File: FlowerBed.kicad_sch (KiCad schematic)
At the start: 28 parts, among them J1 Conn_01x02, J2 AudioJack3_SwitchTR, J3 AudioJack3_SwitchTR, J4 Conn_01x07, J5 Conn_01x16, J6 Conn_01x02, SW0 SW_SPST, SW1 SW_SPST, SW2 SW_SPST, SW3 SW_SPST, SW4 SW_SPST, SW5 SW_SPST, SW6 SW_SPST, SW7 SW_SPST, U1 PAM8302AASCR

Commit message: Legacy active sum
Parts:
- removed R1, R2: 1k, Resistor_SMD:R_01005_0402Metric, symbol Device:R_US
- added C5, C6, C7: 1uF, symbol Device:C
- added C8: 100n, symbol Device:C
- added J7: USB_C_Receptacle_PowerOnly_6P, symbol Connector:USB_C_Receptacle_PowerOnly_6P
- added R10, R7, R8, R9: 20k, Resistor_SMD:R_01005_0402Metric, symbol Device:R_US
- added R12: 1Meg, Resistor_SMD:R_01005_0402Metric, symbol Device:R_US
- added R13: 50, Resistor_SMD:R_01005_0402Metric, symbol Device:R_US
- added R14: 10k, Resistor_SMD:R_01005_0402Metric, symbol Device:R_US
- added R4: 150, symbol Device:R_US
- added R5, R6: 5.1k, symbol Device:R_US
- added U2: TPS2115ADRBR, Package_TO_SOT_SMD:SOT-583-8, symbol Flowerbed:TPS2115ADRBR
- added U4: TLV271CDBVR, Package_TO_SOT_SMD:SOT-353_SC-70-5, symbol Amplifier_Operational:TLV172IDCK
- A1, J1, J2, J3, J4, J5, J6, POT0, POT1, POT2, POT3, SW0, SW1, SW2, SW3, SW4, SW5, SW6, SW7: now fitted
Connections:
- net 3V3_A: now also C6.1, R9.2, U2.2 (D0), U2.8 (IN1), U4.5 (V+)
- net GND: now also C5.2, C6.2, C7.2, J7.A12 (GND), J7.B12 (GND), J7.S1 (SHIELD), R10.1, R12.1, R4.2, R5.1, R6.1, U2.3 (D1), U2.5 (GND), U4.2 (V-)
- net LINEOUT_MONO: now also R13.1
- net Vin: now also C7.1, J7.A9 (VBUS), J7.B9 (VBUS), U2.7 (OUT)
- net at J2.RN: now also R8.2
- net at J2.TN: now also R7.2
- new net: C8.2, R13.2
- new net: R4.1, U2.4 (ILIM)
- new net: R14.2, R7.1, R8.1, U4.1 (+)
- new net: C8.1, R12.2, U4.3 (-), U4.4
- new net: J7.A5 (CC1), R5.2
- new net: J7.B5 (CC2), R6.2
- new net 1v65: R10.2, R14.1, R9.1
- new net IN_5V: C5.1, U2.6 (IN2)
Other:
- note added: "5V USB-C Input & Power Mux"
- note added: "Audio I/O & Mono Summing Amp"
- note added: "Class-D Amp"
- note added: "Daisy Breakouts"
- note added: "GPIO"
- moved on the sheet: C1, C2, C3, R3, U1, VR1

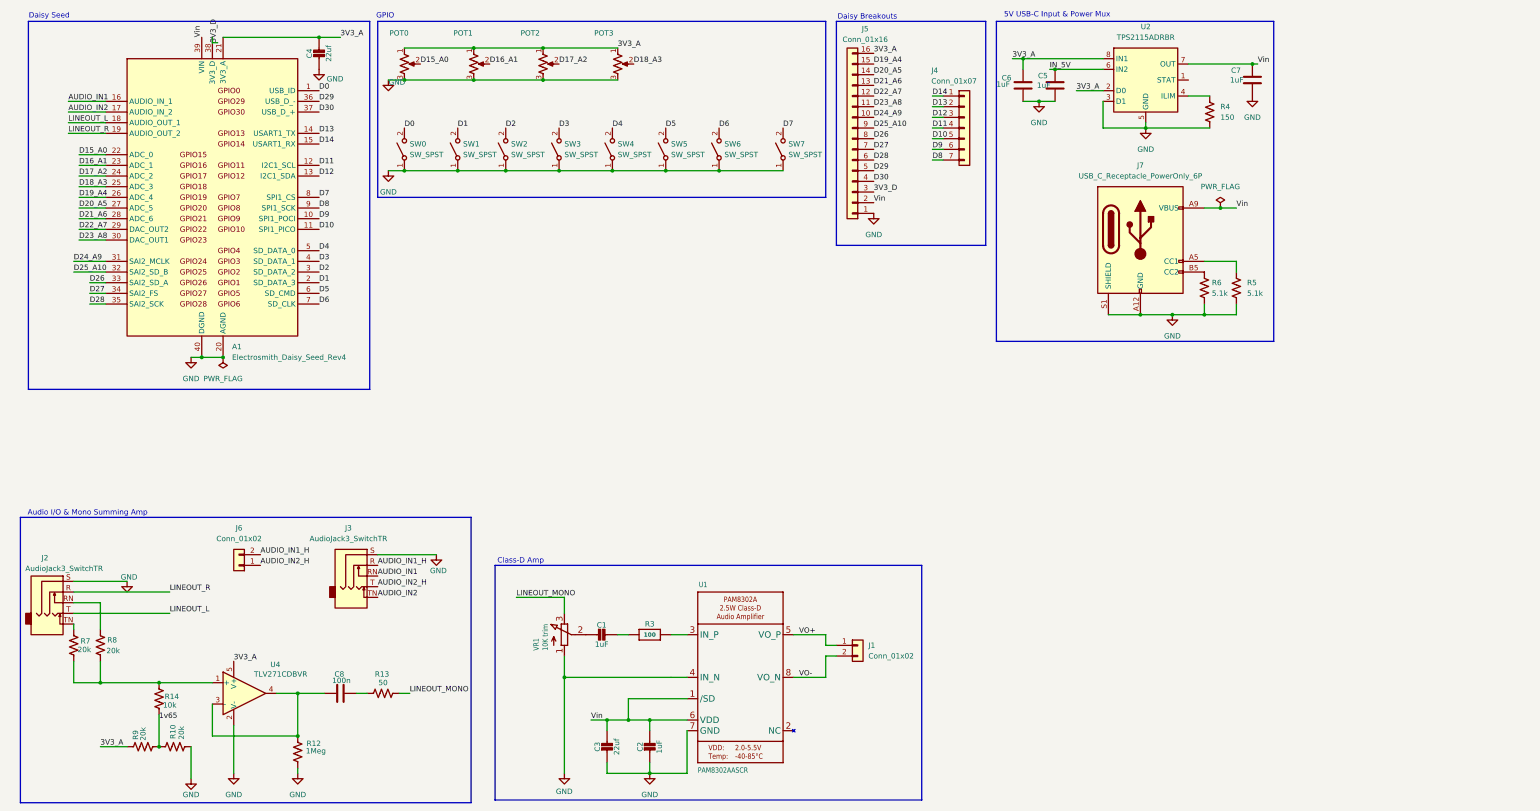
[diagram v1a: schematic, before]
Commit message: Make sum passive, add manuals
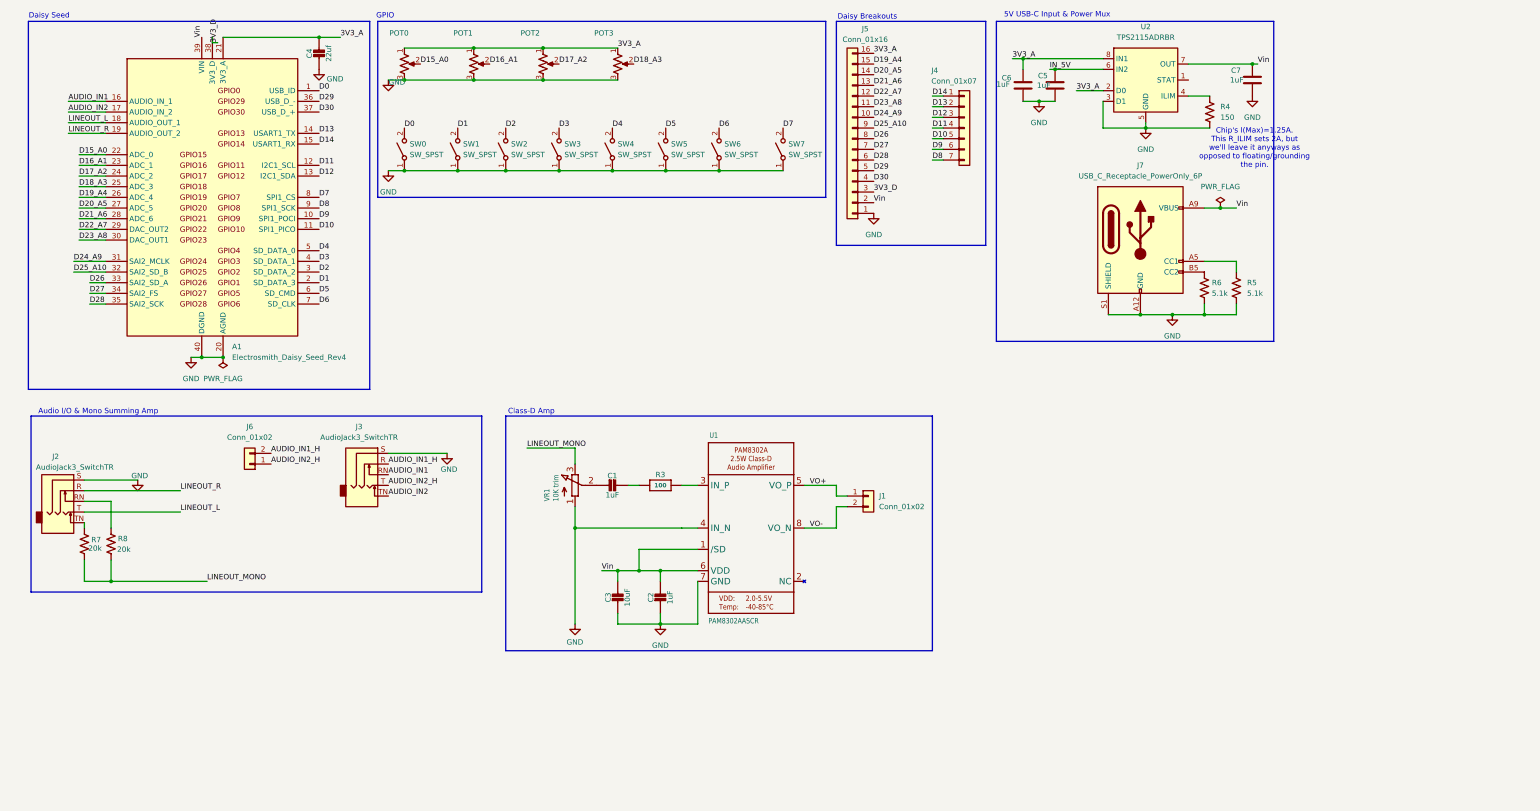
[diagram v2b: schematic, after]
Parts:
- removed C8: 100n, symbol Device:C
- removed R10, R9: 20k, Resistor_SMD:R_01005_0402Metric, symbol Device:R_US
- removed R12: 1Meg, Resistor_SMD:R_01005_0402Metric, symbol Device:R_US
- removed R13: 50, Resistor_SMD:R_01005_0402Metric, symbol Device:R_US
- removed R14: 10k, Resistor_SMD:R_01005_0402Metric, symbol Device:R_US
- removed U4: TLV271CDBVR, Package_TO_SOT_SMD:SOT-353_SC-70-5, symbol Amplifier_Operational:TLV172IDCK
- C3: value 22uf -> 10uF
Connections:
- net LINEOUT_MONO: now also R7.1, R8.1
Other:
- note added: "Chip's I(Max)=1.25A. This R_ILIM sets 2A, but we'll leave it anyways as opposed to floating/grounding the pin."
- moved on the sheet: C1, C2, C3, J1, J2, J3, J6, R3, R7, R8, U1, VR1

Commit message: Update footprints for ICs
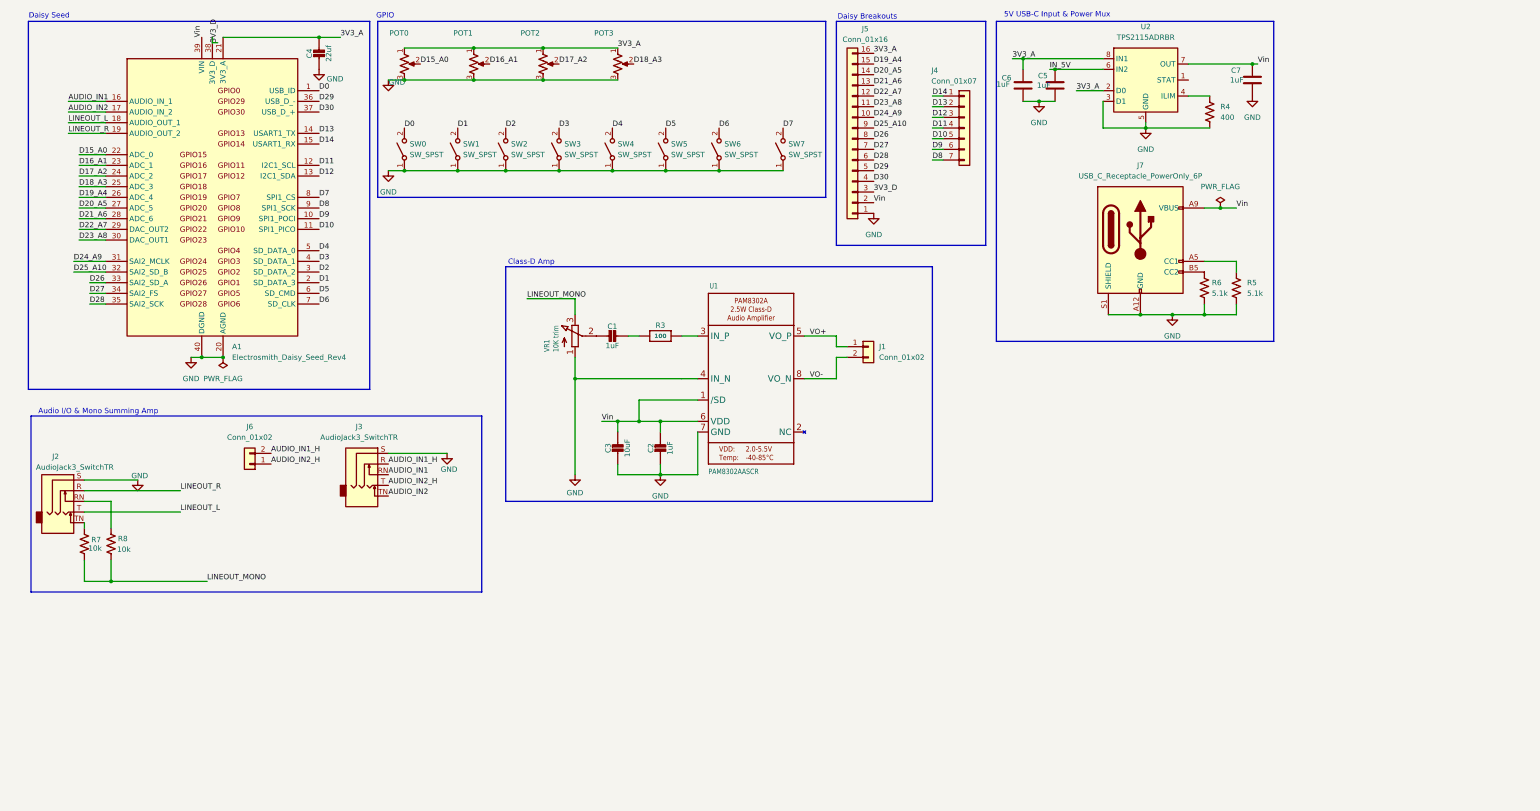
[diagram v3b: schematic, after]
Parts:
- J7: footprint (none) -> Flowerbed:TYPE-C-31-M-12
- R4: value 150 -> 400
- R7, R8: value 20k -> 10k
- U2: footprint Package_TO_SOT_SMD:SOT-583-8 -> Package_SON:SON-8-1EP_3x2mm_P0.5mm_EP1.4x1.6mm
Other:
- note removed: "Chip's I(Max)=1.25A. This R_ILIM sets 2A, but we'll leave it anyways as opposed to floating/grounding the pin."
- moved on the sheet: C1, C2, C3, J1, R3, U1, VR1

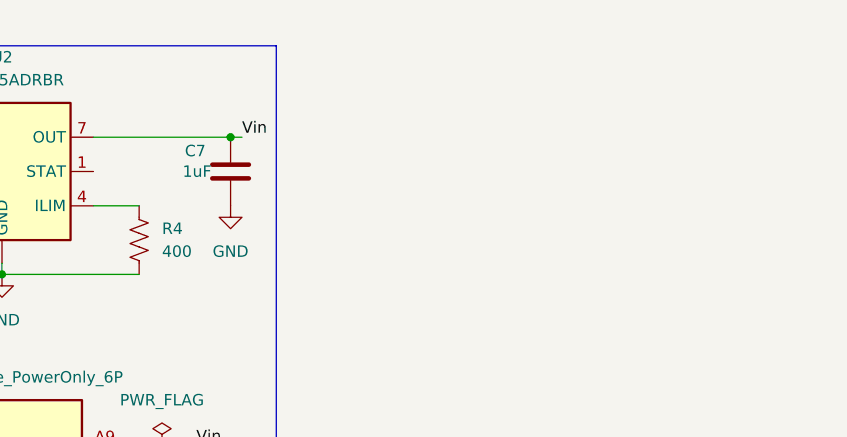
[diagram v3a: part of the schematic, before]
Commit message: Update footprints for passives
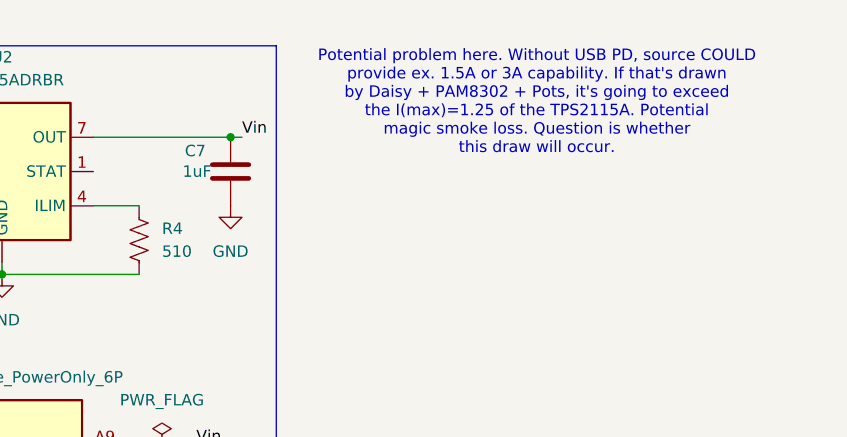
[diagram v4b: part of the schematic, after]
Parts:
- C1, C2: footprint Capacitor_SMD:C_0402_1005Metric -> Capacitor_SMD:C_0201_0603Metric
- C3: footprint Capacitor_SMD:C_0805_2012Metric -> Capacitor_SMD:C_01005_0402Metric
- C4: footprint Capacitor_SMD:C_0805_2012Metric -> Capacitor_SMD:C_1206_3216Metric
- C5, C6, C7: footprint (none) -> Capacitor_SMD:C_0201_0603Metric
- R3: footprint Resistor_SMD:R_0402_1005Metric -> Resistor_SMD:R_0805_2012Metric
- R4: value 400 -> 510; footprint (none) -> Resistor_SMD:R_0805_2012Metric
- R5, R6: footprint (none) -> Resistor_SMD:R_0201_0603Metric
- R7, R8: footprint Resistor_SMD:R_01005_0402Metric -> Resistor_SMD:R_0805_2012Metric
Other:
- note added: "Potential problem here. Without USB PD, source COULD provide ex. 1.5A or 3A capability. If that's drawn by Daisy + PAM8302 + Pots, it's going to exceed the I(max)=1.25 of the TPS2115A. Potential magic smoke loss. Question is whether this draw will occur."
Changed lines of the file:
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@@
 		)
 	)
+	(text "Potential problem here. Without USB PD, source COULD \nprovide ex. 1.5A or 3A capability. If that's drawn\nby Daisy + PAM8302 + Pots, it's going to exceed\nthe I(max)=1.25 of the TPS2115A. Potential\nmagic smoke loss. Question is whether\nthis draw will occur.\n"
+		(exclude_from_sim no)
+		(at 342.646 26.67 0)
+		(effects
+			(font
+				(size 1.27 1.27)
+			)
+		)
+	)
 	(text "5V USB-C Input & Power Mux"
 		(exclude_from_sim no)
@@
 			)
 		)
-		(property "Footprint" "Capacitor_SMD:C_0402_1005Metric"
+		(property "Footprint" "Capacitor_SMD:C_0201_0603Metric"
 			(at 154.94 95.25 0)
 			(hide yes)
@@
 			)
 		)
-		(property "Description" "C14445"
+		(property "Description" "C15849"
 			(at 154.94 95.25 0)
 			(hide yes)
@@
 			)
 		)
-		(property "Footprint" ""
+		(property "Footprint" "Capacitor_SMD:C_0201_0603Metric"
 			(at 254.9652 39.37 0)
 			(hide yes)
@@
 			)
 		)
-		(property "Description" "Unpolarized capacitor"
+		(property "Description" "C15849"
 			(at 254 35.56 0)
 			(hide yes)
@@
 			)
 		)
-		(property "Footprint" "Capacitor_SMD:C_0402_1005Metric"
+		(property "Footprint" "Capacitor_SMD:C_0201_0603Metric"
 			(at 167.64 123.19 0)
 			(hide yes)
@@
 			)
 		)
-		(property "Description" "C14445"
+		(property "Description" "C15849"
 			(at 167.64 123.19 0)
 			(hide yes)
@@
 			)
 		)
-		(property "Value" "400"
+		(property "Value" "510"
 			(at 300.99 43.1799 0)
 			(show_name no)
@@
 			)
 		)
-		(property "Footprint" ""
+		(property "Footprint" "Resistor_SMD:R_0805_2012Metric"
 			(at 299.466 42.164 90)
 			(hide yes)
@@
 			)
 		)
-		(property "Description" "Resistor, US symbol"
+		(property "Description" "C17734"
 			(at 298.45 41.91 0)
 			(hide yes)
@@
 			)
 		)
-		(property "Footprint" ""
+		(property "Footprint" "Capacitor_SMD:C_0201_0603Metric"
 			(at 309.5752 38.1 0)
 			(hide yes)
@@
 			)
 		)
-		(property "Description" "Unpolarized capacitor"
+		(property "Description" "C15849"
 			(at 308.61 34.29 0)
 			(hide yes)
@@
 			)
 		)
-		(property "Footprint" "Resistor_SMD:R_01005_0402Metric"
+		(property "Footprint" "Resistor_SMD:R_0805_2012Metric"
 			(at 29.464 144.526 90)
 			(hide yes)
@@
 			)
 		)
-		(property "Description" "Resistor, US symbol"
+		(property "Description" "C17414"
 			(at 30.48 144.78 0)
 			(hide yes)
@@
 			)
 		)
-		(property "Description" "USB Power-Only 6P Type-C Receptacle connector"
+		(property "Description" "C165948"
 			(at 281.94 72.39 0)
 			(hide yes)
@@
 			)
 		)
-		(property "Footprint" ""
+		(property "Footprint" "Capacitor_SMD:C_0201_0603Metric"
 			(at 262.5852 39.37 0)
 			(hide yes)
@@
 			)
 		)
-		(property "Description" "Unpolarized capacitor"
+		(property "Description" "C15849"
 			(at 261.62 35.56 0)
 			(hide yes)
@@
 			)
 		)
-		(property "Footprint" "Capacitor_SMD:C_0805_2012Metric"
+		(property "Footprint" "Capacitor_SMD:C_01005_0402Metric"
 			(at 157.48 123.19 0)
 			(hide yes)
@@
 			)
 		)
-		(property "Description" "C76636"
+		(property "Description" "C15525"
 			(at 157.48 123.19 0)
 			(hide yes)
@@
 			)
 		)
-		(property "Footprint" "Resistor_SMD:R_01005_0402Metric"
+		(property "Footprint" "Resistor_SMD:R_0805_2012Metric"
 			(at 35.814 144.526 90)
 			(hide yes)
@@
 			)
 		)
-		(property "Description" "Resistor, US symbol"
+		(property "Description" "C17414"
 			(at 36.83 144.78 0)
 			(hide yes)
@@
 			)
 		)
-		(property "Footprint" "Resistor_SMD:R_0402_1005Metric"
+		(property "Footprint" "Resistor_SMD:R_0805_2012Metric"
 			(at 167.64 95.25 0)
 			(hide yes)
@@
 			)
 		)
-		(property "Description" "C173685"
+		(property "Description" "C17408"
 			(at 167.64 95.25 0)
 			(hide yes)
@@
 			)
 		)
-		(property "Footprint" ""
+		(property "Footprint" "Resistor_SMD:R_0201_0603Metric"
 			(at 303.784 83.566 90)
 			(hide yes)
@@
 			)
 		)
-		(property "Description" "Resistor, US symbol"
+		(property "Description" "C23186"
 			(at 304.8 83.82 0)
 			(hide yes)
@@
 			)
 		)
-		(property "Footprint" "Capacitor_SMD:C_0805_2012Metric"
+		(property "Footprint" "Capacitor_SMD:C_1206_3216Metric"
 			(at 86.36 29.21 0)
 			(hide yes)
@@
 			)
 		)
-		(property "Description" "C76636"
+		(property "Description" "C12891"
 			(at 86.36 29.21 0)
 			(hide yes)
@@
 			)
 		)
-		(property "Footprint" ""
+		(property "Footprint" "Resistor_SMD:R_0201_0603Metric"
 			(at 296.164 83.566 90)
 			(hide yes)
@@
 			)
 		)
-		(property "Description" "Resistor, US symbol"
+		(property "Description" "C23186"
 			(at 297.18 83.82 0)
 			(hide yes)
